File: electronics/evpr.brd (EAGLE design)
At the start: 97.2 x 41.3 mm, 120 parts, among them J1 10118193-0001LF, J2 B4P-VH(LF)(SN), Q1 AOD4184A, Q2 AOD4184A, T1 MMBT2222A, T2 MMBT2222A, T3 MMBT2222A, T5 MMBT2222A, U1 MC14044BDR2G, U2 BQ2057TTS, U3 ESP32-WROOM-32D, U5 AP2112K-3.3TRG1, U6 SN74AHCT125DR, U7 TPSM84824MOLR, U8 LTC4353CMSPBFMSOP-16_MS-M, X1 B3P-VH(LF)(SN), X2 B3P-VH(LF)(SN), X3 B3P-VH(LF)(SN)

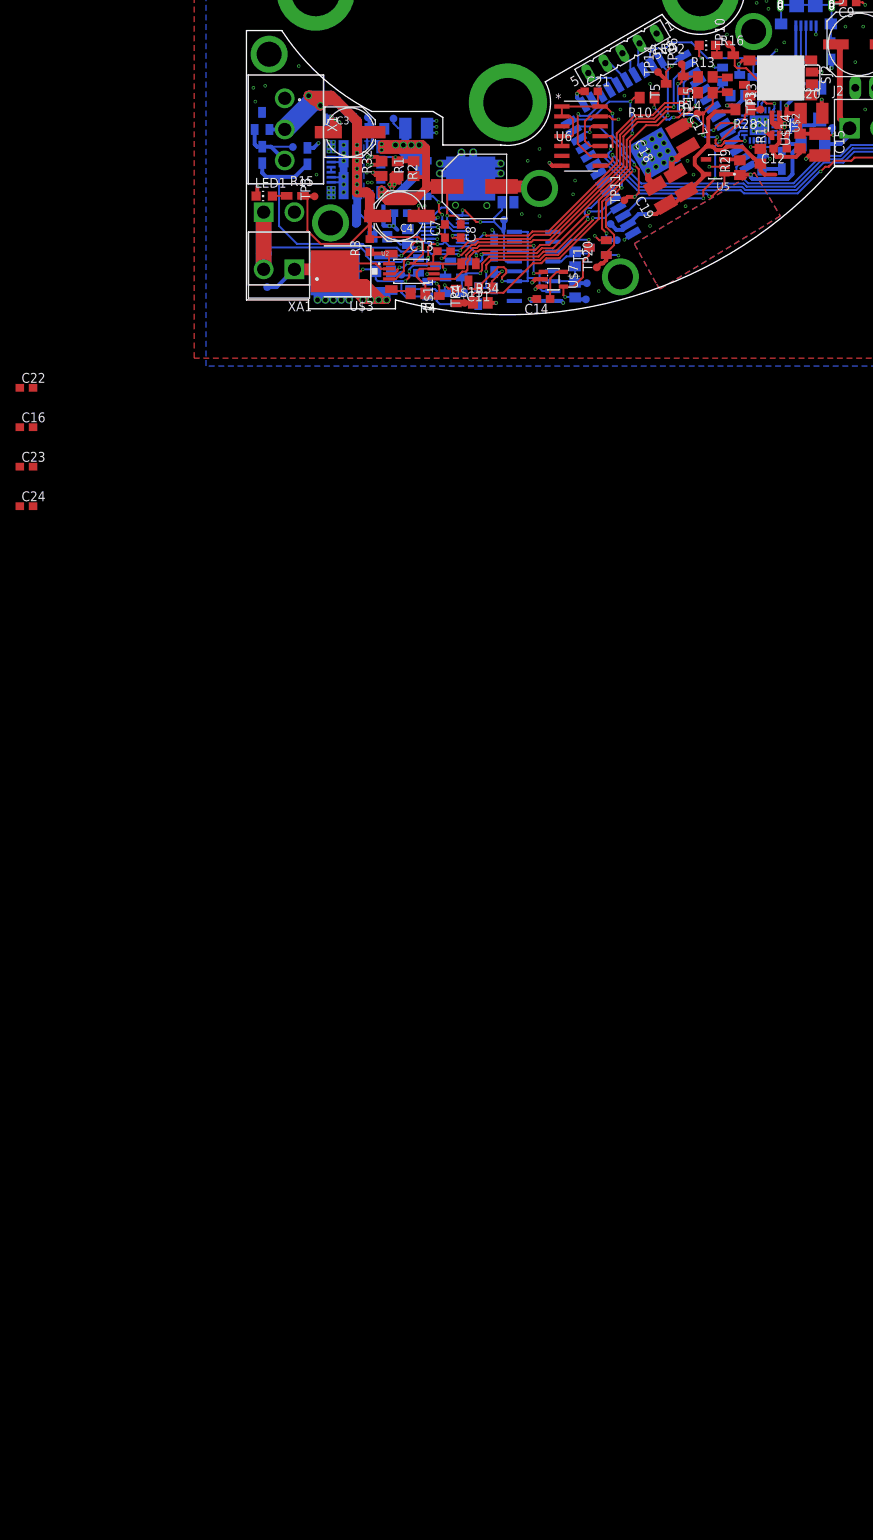
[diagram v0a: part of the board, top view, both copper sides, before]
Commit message: Completely redid sub 8V power path to support ESP32 deep-sleep as primary powersave mechagnism.
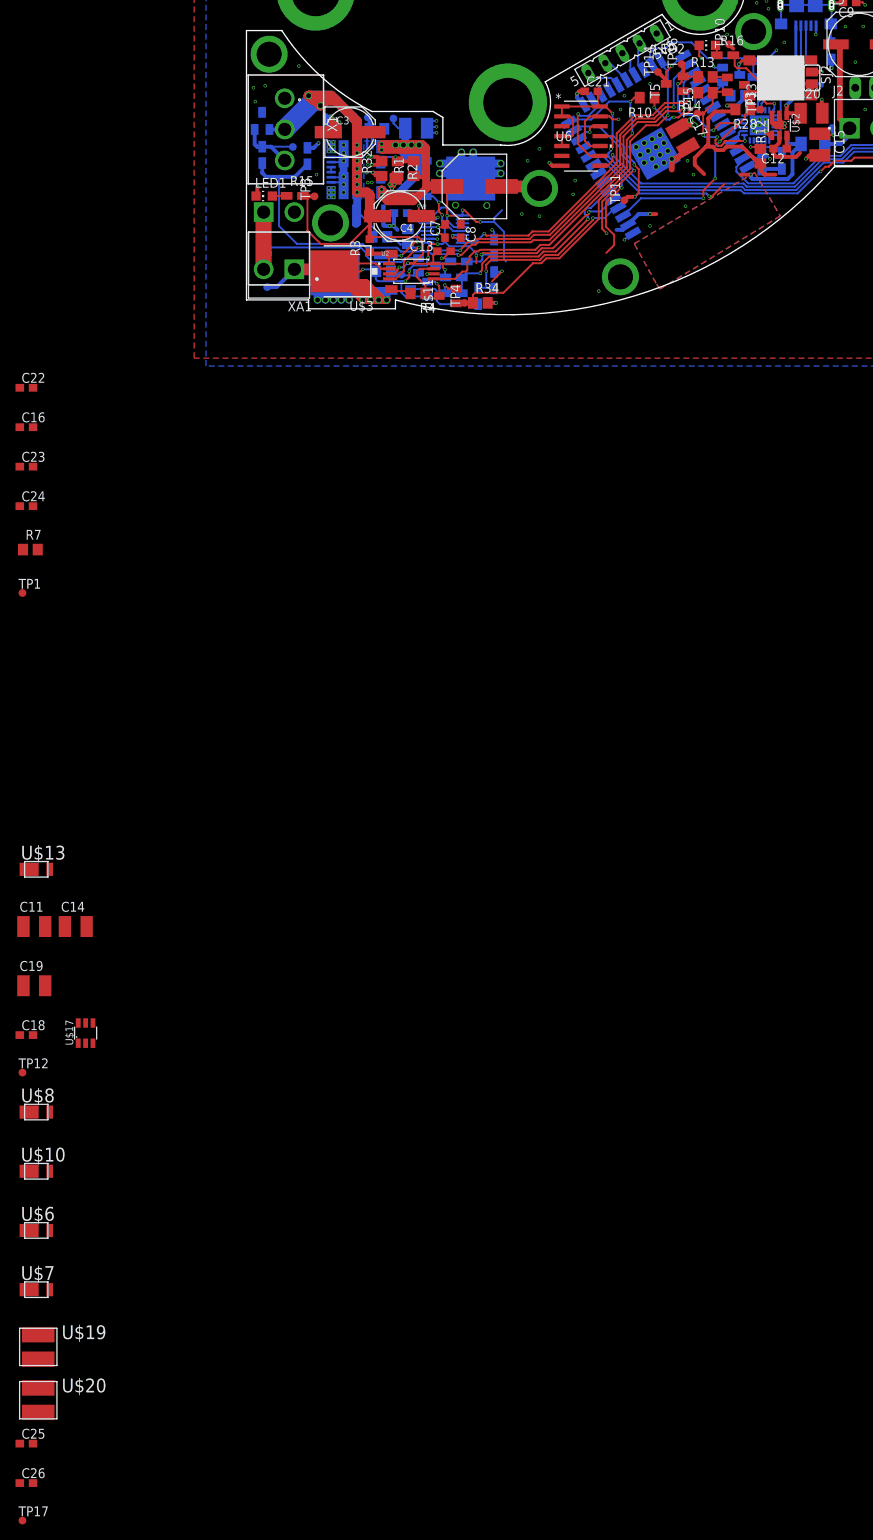
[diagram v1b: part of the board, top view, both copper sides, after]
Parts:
- removed R29, R8: 100k, rcl:R0805
- removed SJ1: (no value), jumper:SJ
- removed T1, T2: MMBT2222A, transistor-neu-to92:SOT23-BEC
- removed TP19, TP20, TP21, TP22, TP23: PTR1TP10R, testpad:TP10R
- removed U$14: 4.7µH, mccloud:R0805
- removed U1: MC14044BDR2G, mccloud:SOIC-16
- removed U5: AP2112K-3.3TRG1, mccloud:SOT95P285X140-5N
- added C25, C26: 0.1uF, eagle-ltspice:C0603
- added TP1, TP17: PTR1TP10R, testpad:TP10R
- added U$17: (no value), mccloud:TSOT23-6
- added U$19: 3.9µH, mccloud:SRR4818A-XXXX
- added U$20: 4.7µH, mccloud:SRR4818A-XXXX
- added U$6: SMD34LHE1, mccloud:SOD-123HE1
- C11: value 0.1uF -> 22uF; device eagle-ltspice:C0603 -> eagle-ltspice:C1210
- C14: value 0.01uF -> 10uF; device eagle-ltspice:C0603 -> eagle-ltspice:C1210
- C18: value 10uF -> 0.1uF; device eagle-ltspice:C1210 -> eagle-ltspice:C0603
- C19: value 1uF -> 22uF
- R7: value 100k -> 10k
- U$10, U$8: value LSM115J -> SMD34LHE1; device mccloud:DO214BA -> mccloud:SOD-123HE1
- U$13: value SDM40E20LC -> SMD34LHE1; device mccloud:SOT23 -> mccloud:SOD-123HE1
- U$7: value R3119N050A-TR-FE -> SMD34LHE1; device mccloud:SOT23-5 -> mccloud:SOD-123HE1
- moved U$10 170.4 mm to (-60.7, -166.1), flipped to the top, turned to 0 degrees
- moved U$8 161.9 mm to (-60.7, -158.5), flipped to the top, turned to 0 degrees
- moved U$7 146.1 mm to (-60.7, -181.4), turned to 0 degrees
- moved C18 138.3 mm to (-62.0, -148.6), turned to 0 degrees
- moved TP12 132.9 mm to (-62.5, -153.4), flipped to the top, turned to 0 degrees
- moved C19 129.8 mm to (-61.0, -142.2), turned to 0 degrees
- moved C11 100.8 mm to (-61.0, -134.6), turned to 0 degrees
- moved C14 100.7 mm to (-55.6, -134.6), turned to 0 degrees
- moved U$13 94.9 mm to (-60.7, -127.3), turned to 0 degrees
- moved R7 79.5 mm to (-61.5, -86.1), flipped to the top, turned to 0 degrees
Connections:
- removed net 3.3V: C18.1, C19.1, R28.1, R9.1, TP12.TP, U3.2, U5.5
- removed net N$11: R8.1, T1.C, TP22.TP, U$7.4, U1.3
- removed net N$12: R7.1, T2.C, U1.4
- removed net N$30: SJ1.2, TP21.TP, U1.13, U8.1, U8.16
- removed net N$43: C11.2, R7.2, R8.2, TP23.TP, U$13.3, U1.11, U1.12, U1.14, U1.15, U1.16, U1.5, U1.6, U1.7
- removed net N$9: C14.1, U$7.5
- new net BUILTIN_LED: R16.2
- new net ESP_POWER: C11.1, C19.1, R28.1, R7.1, R9.1, TP12.TP, U$17.1, U$19.P$2, U3.2
- new net LED_BUILTIN: U3.14
- new net N$14: C18.1, U$17.6
- new net N$41: C14.1, C25.2, TP17.TP, U$10.C, U$13.C, U$17.2, U$17.3, U$8.C
- new net SYS_POW_EN: R7.2, TP1.TP, U8.1, U8.16
- net 5.0V: now also U$6.C, U$7.C; no longer R29.1, U$10.C, U$8.C, U5.1
- net CSTAT: no longer U3.14
- net GND: now also C11.2, C25.1, C26.1, U$17.4; no longer C11.1, C18.2, SJ1.1, T1.E, T2.E, U$7.2, U$7.3, U1.8, U5.2
- net N$26: now also C18.2, U$17.5, U$19.P$1; no longer R29.2, U5.3
- net N$47: no longer U3.29
- net N$50: now also U$20.P$1; no longer U$14.1
- net N$51: now also U$20.P$2, U$7.A; no longer U$14.2, U$8.A
- net SHUTDOWN: no longer T2.B, TP19.TP
- net SHUTDOWN_CANCEL: no longer T1.B, TP20.TP
- net SYS_POWER: now also C26.2
- net VBAT: now also U$13.A; no longer U$13.1
- net VCONV: now also U$8.A
- net VRAW: no longer U$13.2, U$7.1
- net VUSB: now also U$6.A; no longer R16.2
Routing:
- net 3.3V: track 49.2 -> 0.00 mm, vias 4 -> 0
- net N$43: track 41.0 -> 0.00 mm, vias 1 -> 0
- net ESP_POWER: track 0.00 -> 39.2 mm, vias 0 -> 4
- net N$30: track 22.0 -> 0.00 mm, vias 2 -> 0
- net N$11: track 18.7 -> 0.00 mm, vias 2 -> 0
- net SYS_POW_EN: track 0.00 -> 18.4 mm, vias 0 -> 2
- net GND: track 115.5 -> 98.4 mm, vias 133 -> 125
- net VRAW: track 138.4 -> 122.8 mm, vias 14 -> 12
- net 5.0V: track 68.7 -> 60.5 mm
- net N$12: track 7.31 -> 0.00 mm
- net N$51: track 13.3 -> 7.90 mm
- net N$9: track 4.71 -> 0.00 mm
- net SHUTDOWN_CANCEL: track 18.3 -> 15.8 mm
- net SHUTDOWN: track 23.4 -> 21.2 mm
- net N$26: track 2.05 -> 0.00 mm
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
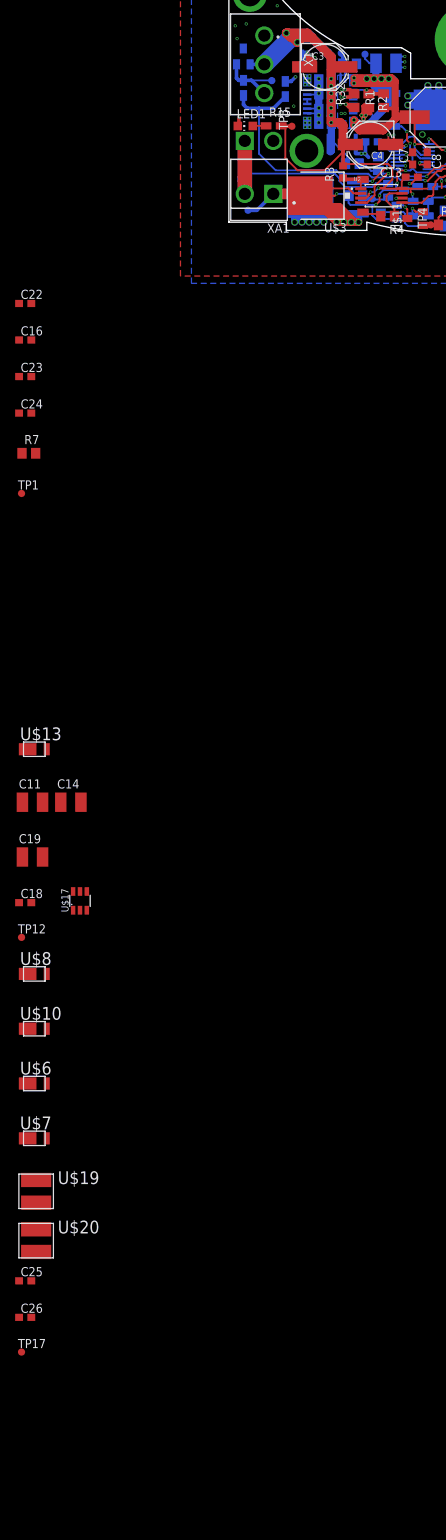
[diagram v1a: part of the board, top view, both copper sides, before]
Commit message: Switched C3 and C4 to alternative capacitor
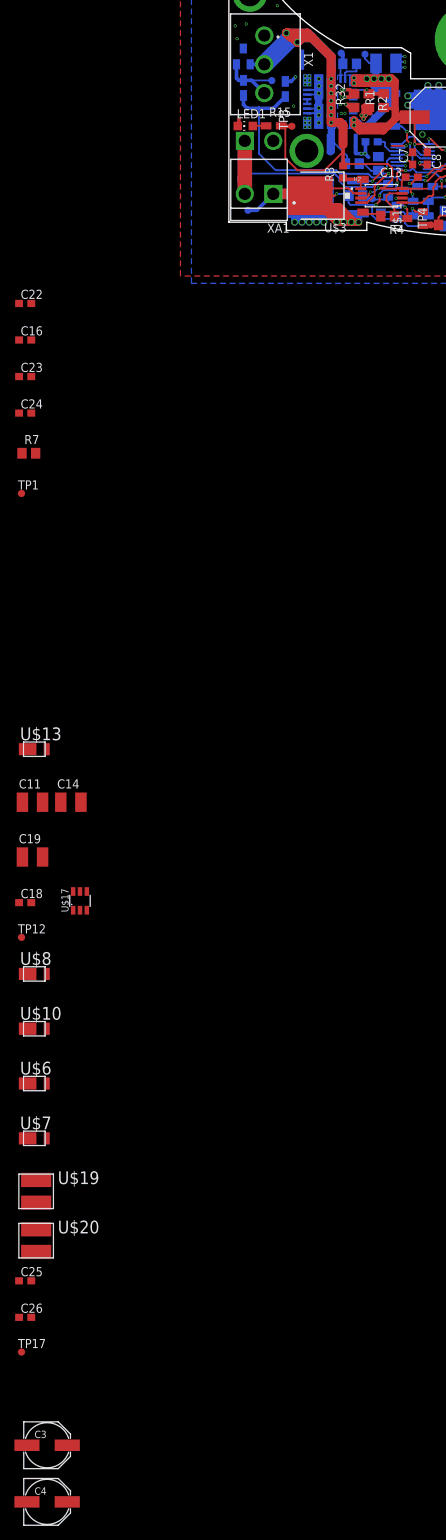
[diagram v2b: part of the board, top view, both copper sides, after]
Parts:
- moved C3 195.5 mm to (-58.9, -224.0)
- moved C4 194.0 mm to (-58.9, -231.9), turned to 0 degrees
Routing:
- net GND: track 98.4 -> 85.6 mm, vias 125 -> 120
- net VRAW: track 122.8 -> 120.3 mm

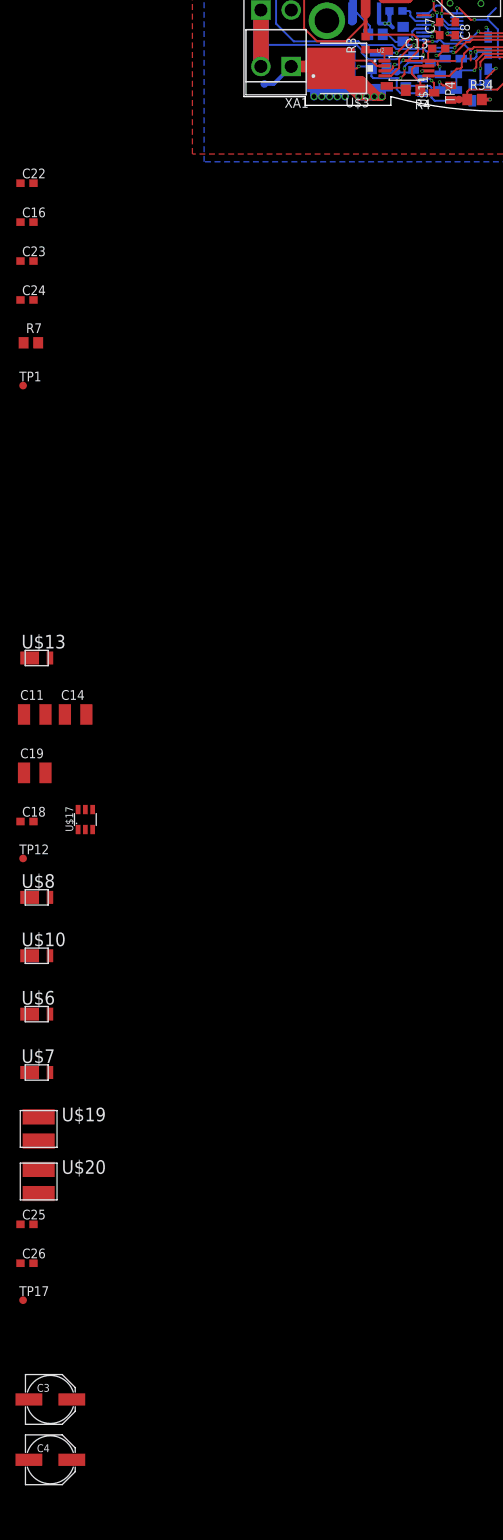
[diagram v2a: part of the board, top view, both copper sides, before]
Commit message: Altered Battery Charge Symbol and cleaned up battery charge schematic
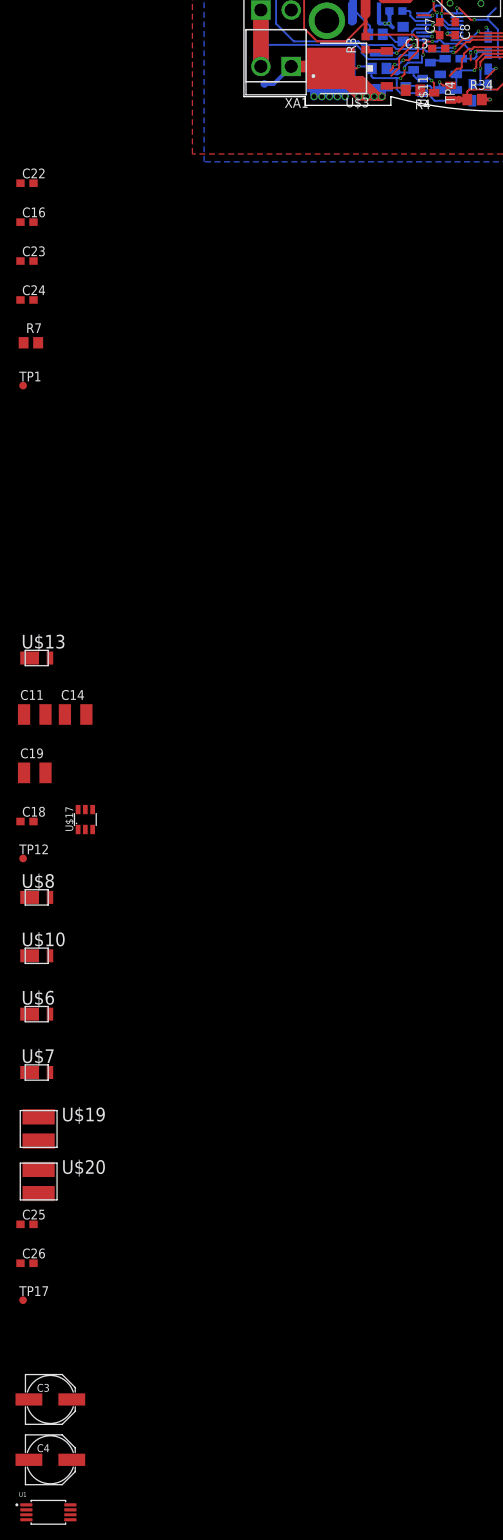
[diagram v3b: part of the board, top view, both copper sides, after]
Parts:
- removed U2: BQ2057TTS, BQ2057TTS:SOP65P640X120-8N
- added U1: BQ2057TTS, mccloud:SOP65P640X120-8N
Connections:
- removed net N$2: R4.1, U2.7
- new net N$9: R4.1, U1.7
- net CSTAT: now also U1.5; no longer U2.5
- net GND: now also U1.6; no longer U2.6
- net N$5: now also U1.1; no longer U2.1
- net N$7: now also U1.4; no longer U2.4
- net VBAT: now also U1.2; no longer U2.2
- net VRAW: now also U1.3, U1.8; no longer U2.3, U2.8
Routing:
- net VRAW: track 120.3 -> 109.2 mm, vias 12 -> 11
- net VBAT: track 94.7 -> 86.8 mm
- net N$2: track 5.58 -> 0.00 mm
- net CSTAT: track 50.5 -> 47.7 mm
- net GND: track 85.6 -> 83.2 mm, vias 120 -> 118
- net N$5: track 4.27 -> 3.27 mm
- net N$7: track 11.1 -> 10.2 mm
